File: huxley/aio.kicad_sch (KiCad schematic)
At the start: 61 parts, among them J11 SMA_RF2-04A-T-00-50-G, J13 SMA_RF2-04A-T-00-50-G, J15 SMA_RF2-04A-T-00-50-G, J17 SMA_RF2-04A-T-00-50-G, J18 SMA_RF2-04A-T-00-50-G, J19 SMA_RF2-04A-T-00-50-G, J20 SMA_RF2-04A-T-00-50-G, J22 SMA_RF2-04A-T-00-50-G, J24 CT3151V1-2, J39 CT3151V1-2, J4 SMA_RF2-04A-T-00-50-G, J7 SMA_RF2-04A-T-00-50-G, J9 SMA_RF2-04A-T-00-50-G

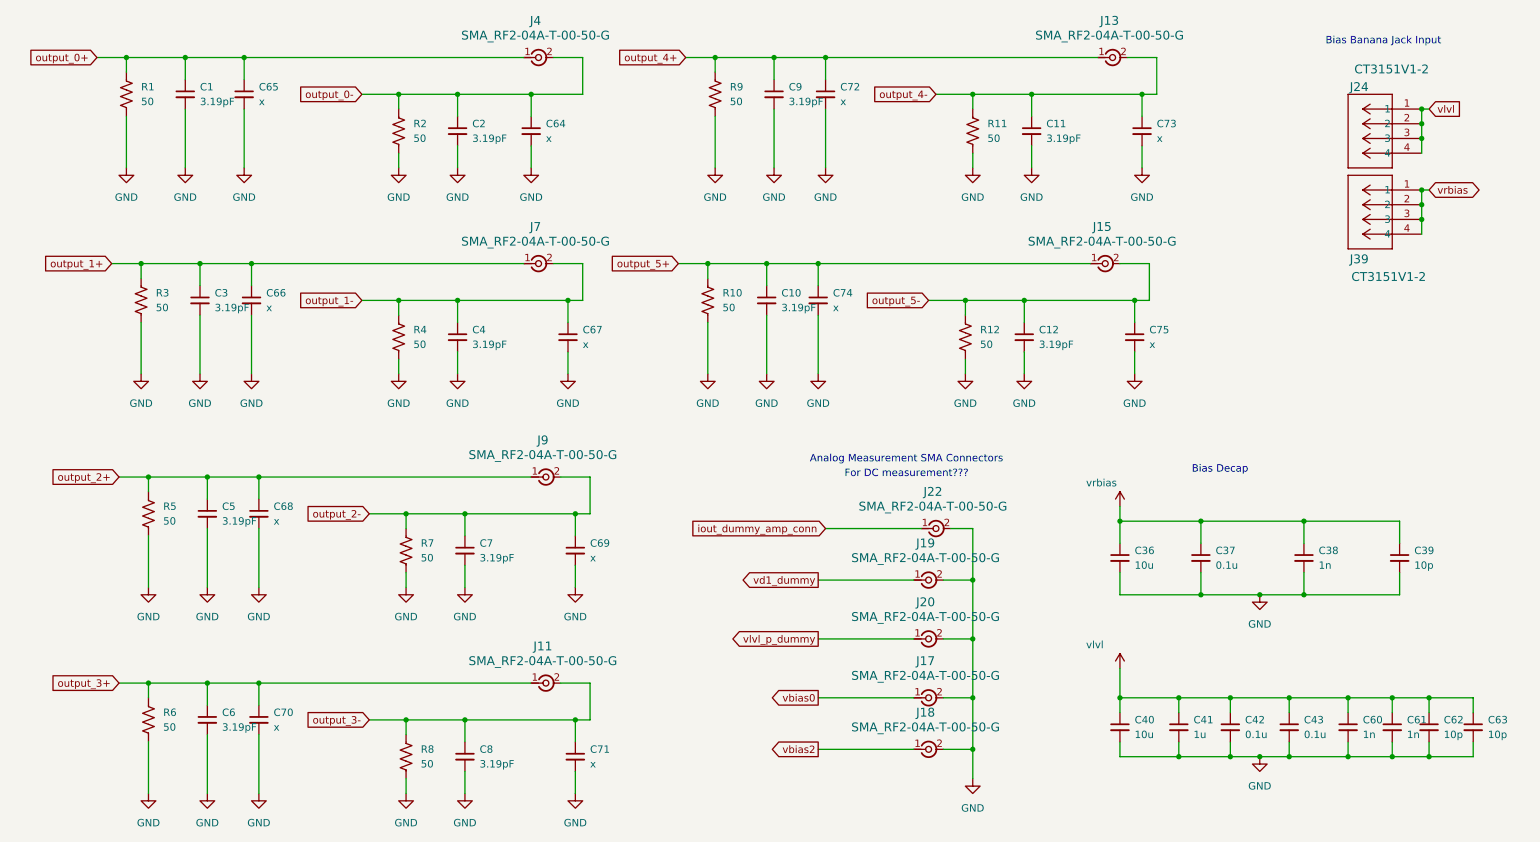
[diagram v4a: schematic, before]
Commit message: added DNP prop to some caps and updated bom; added regular and rounded board outputs
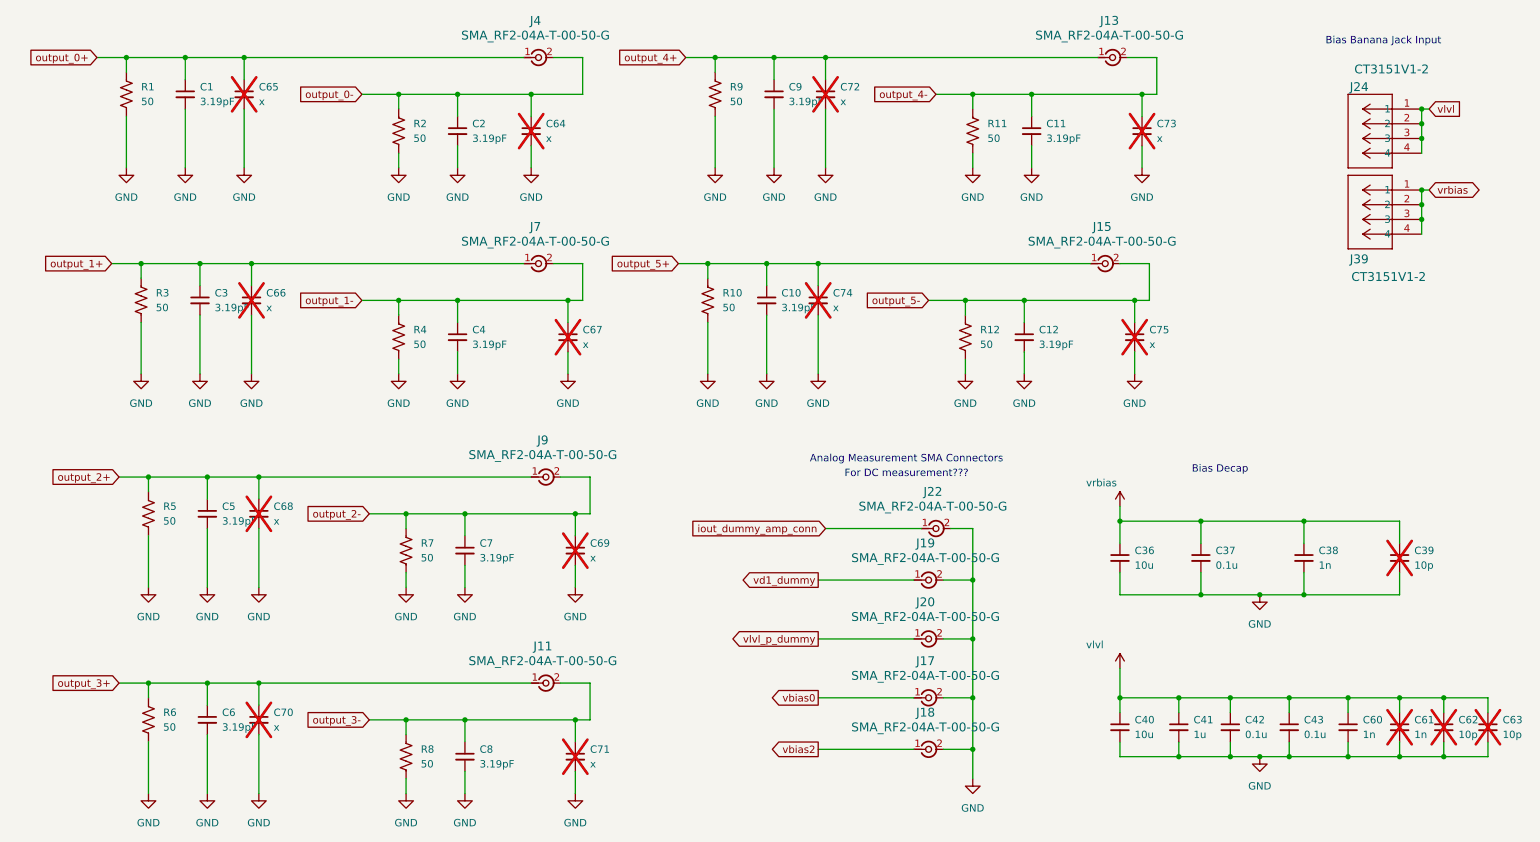
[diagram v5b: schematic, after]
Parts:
- C39, C61, C62, C63, C64, C65, C66, C67, C68, C69, C70, C71, C72, C73, C74, C75: now not fitted
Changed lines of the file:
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@@
 	)
 	(junction
-		(at 255.27 152.4)
+		(at 256.54 152.4)
 		(diameter 0)
 		(color 0 0 0 0)
@@
 	)
 	(junction
-		(at 255.27 142.24)
+		(at 256.54 142.24)
 		(diameter 0)
 		(color 0 0 0 0)
@@
 	)
 	(junction
+		(at 264.16 152.4)
+		(diameter 0)
+		(color 0 0 0 0)
+	)
+	(junction
 		(at 85.09 146.05)
 		(diameter 0)
@@
 	)
 	(junction
+		(at 264.16 142.24)
+		(diameter 0)
+		(color 0 0 0 0)
+	)
+	(junction
 		(at 83.82 38.1)
 		(diameter 0)
@@
 	)
 	(junction
-		(at 261.62 152.4)
-		(diameter 0)
-		(color 0 0 0 0)
-	)
-	(junction
 		(at 260.35 54.61)
 		(diameter 0)
@@
 		(color 0 0 0 0)
 	)
-	(junction
-		(at 261.62 142.24)
-		(diameter 0)
-		(color 0 0 0 0)
-	)
 	(wire
 		(pts
@@
 	(wire
 		(pts
-			(xy 269.24 152.4) (xy 261.62 152.4)
+			(xy 271.78 152.4) (xy 264.16 152.4)
 		)
 		(stroke
@@
 	(wire
 		(pts
-			(xy 247.65 142.24) (xy 255.27 142.24)
+			(xy 247.65 142.24) (xy 256.54 142.24)
 		)
 		(stroke
@@
 	(wire
 		(pts
-			(xy 269.24 142.24) (xy 261.62 142.24)
+			(xy 271.78 142.24) (xy 264.16 142.24)
 		)
 		(stroke
@@
 	(wire
 		(pts
-			(xy 255.27 149.86) (xy 255.27 152.4)
+			(xy 256.54 149.86) (xy 256.54 152.4)
 		)
 		(stroke
@@
 	(wire
 		(pts
-			(xy 269.24 149.86) (xy 269.24 152.4)
+			(xy 271.78 149.86) (xy 271.78 152.4)
 		)
 		(stroke
@@
 	(wire
 		(pts
-			(xy 261.62 149.86) (xy 261.62 152.4)
+			(xy 264.16 149.86) (xy 264.16 152.4)
 		)
 		(stroke
@@
 	(wire
 		(pts
-			(xy 247.65 152.4) (xy 255.27 152.4)
+			(xy 247.65 152.4) (xy 256.54 152.4)
 		)
 		(stroke
@@
 	(wire
 		(pts
-			(xy 255.27 142.24) (xy 261.62 142.24)
+			(xy 256.54 142.24) (xy 264.16 142.24)
 		)
 		(stroke
@@
 	(wire
 		(pts
-			(xy 255.27 144.78) (xy 255.27 142.24)
+			(xy 256.54 144.78) (xy 256.54 142.24)
 		)
 		(stroke
@@
 	(wire
 		(pts
-			(xy 255.27 152.4) (xy 261.62 152.4)
+			(xy 256.54 152.4) (xy 264.16 152.4)
 		)
 		(stroke
@@
 	(wire
 		(pts
-			(xy 269.24 144.78) (xy 269.24 142.24)
+			(xy 271.78 144.78) (xy 271.78 142.24)
 		)
 		(stroke
@@
 	(wire
 		(pts
-			(xy 261.62 144.78) (xy 261.62 142.24)
+			(xy 264.16 144.78) (xy 264.16 142.24)
 		)
 		(stroke
@@
 		(in_bom yes)
 		(on_board yes)
-		(dnp no)
+		(dnp yes)
 		(fields_autoplaced yes)
 		(property "Reference" "C75"
@@
 	(symbol
 		(lib_id "Device:C_Small")
-		(at 261.62 147.32 0)
+		(at 264.16 147.32 0)
 		(unit 1)
 		(exclude_from_sim no)
 		(in_bom yes)
 		(on_board yes)
-		(dnp no)
+		(dnp yes)
 		(fields_autoplaced yes)
 		(property "Reference" "C62"
-			(at 264.16 146.0562 0)
+			(at 266.7 146.0562 0)
 			(effects
 				(font
@@
 		)
 		(property "Value" "10p"
-			(at 264.16 148.5962 0)
+			(at 266.7 148.5962 0)
 			(effects
 				(font
@@
 		)
 		(property "Footprint" "Capacitor_SMD:C_0603_1608Metric"
-			(at 261.62 147.32 0)
+			(at 264.16 147.32 0)
 			(effects
 				(font
@@
 		)
 		(property "Datasheet" "~"
-			(at 261.62 147.32 0)
+			(at 264.16 147.32 0)
 			(effects
 				(font
@@
 		)
 		(property "Description" "Unpolarized capacitor, small symbol"
-			(at 261.62 147.32 0)
+			(at 264.16 147.32 0)
 			(effects
 				(font
@@
 	(symbol
 		(lib_id "Device:C_Small")
-		(at 255.27 147.32 0)
+		(at 256.54 147.32 0)
 		(unit 1)
 		(exclude_from_sim no)
 		(in_bom yes)
 		(on_board yes)
-		(dnp no)
+		(dnp yes)
 		(property "Reference" "C61"
-			(at 257.81 146.0562 0)
+			(at 259.08 146.0562 0)
 			(effects
 				(font
@@
 		)
 		(property "Value" "1n"
-			(at 257.81 148.5962 0)
+			(at 259.08 148.5962 0)
 			(effects
 				(font
@@
 		)
 		(property "Footprint" "Capacitor_SMD:C_0603_1608Metric"
-			(at 255.27 147.32 0)
+			(at 256.54 147.32 0)
 			(effects
 				(font
@@
 		)
 		(property "Datasheet" "~"
-			(at 255.27 147.32 0)
+			(at 256.54 147.32 0)
 			(effects
 				(font
@@
 		)
 		(property "Description" "Unpolarized capacitor, small symbol"
-			(at 255.27 147.32 0)
+			(at 256.54 147.32 0)
 			(effects
 				(font
@@
 	(symbol
 		(lib_id "Device:C_Small")
-		(at 269.24 147.32 0)
+		(at 271.78 147.32 0)
 		(unit 1)
 		(exclude_from_sim no)
 		(in_bom yes)
 		(on_board yes)
-		(dnp no)
+		(dnp yes)
 		(fields_autoplaced yes)
 		(property "Reference" "C63"
-			(at 271.78 146.0562 0)
+			(at 274.32 146.0562 0)
 			(effects
 				(font
@@
 		)
 		(property "Value" "10p"
-			(at 271.78 148.5962 0)
+			(at 274.32 148.5962 0)
 			(effects
 				(font
@@
 		)
 		(property "Footprint" "Capacitor_SMD:C_0603_1608Metric"
-			(at 269.24 147.32 0)
+			(at 271.78 147.32 0)
 			(effects
 				(font
@@
 		)
 		(property "Datasheet" "~"
-			(at 269.24 147.32 0)
+			(at 271.78 147.32 0)
 			(effects
 				(font
@@
 		)
 		(property "Description" "Unpolarized capacitor, small symbol"
-			(at 269.24 147.32 0)
+			(at 271.78 147.32 0)
 			(effects
 				(font
@@
 		(in_bom yes)
 		(on_board yes)
-		(dnp no)
+		(dnp yes)
 		(fields_autoplaced yes)
 		(property "Reference" "C72"
@@
 		(in_bom yes)
 		(on_board yes)
-		(dnp no)
+		(dnp yes)
 		(fields_autoplaced yes)
 		(property "Reference" "C68"
@@
 		(in_bom yes)
 		(on_board yes)
-		(dnp no)
+		(dnp yes)
 		(fields_autoplaced yes)
 		(property "Reference" "C64"
@@
 		(in_bom yes)
 		(on_board yes)
-		(dnp no)
+		(dnp yes)
 		(fields_autoplaced yes)
 		(property "Reference" "C66"
@@
 		(in_bom yes)
 		(on_board yes)
-		(dnp no)
+		(dnp yes)
 		(fields_autoplaced yes)
 		(property "Reference" "C67"
@@
 		(in_bom yes)
 		(on_board yes)
-		(dnp no)
+		(dnp yes)
 		(fields_autoplaced yes)
 		(property "Reference" "C71"
@@
 		(in_bom yes)
 		(on_board yes)
-		(dnp no)
+		(dnp yes)
 		(fields_autoplaced yes)
 		(property "Reference" "C39"
@@
 		(in_bom yes)
 		(on_board yes)
-		(dnp no)
+		(dnp yes)
 		(fields_autoplaced yes)
 		(property "Reference" "C73"
@@
 		(in_bom yes)
 		(on_board yes)
-		(dnp no)
+		(dnp yes)
 		(fields_autoplaced yes)
 		(property "Reference" "C69"
@@
 		(in_bom yes)
 		(on_board yes)
-		(dnp no)
+		(dnp yes)
 		(fields_autoplaced yes)
 		(property "Reference" "C65"
@@
 		(in_bom yes)
 		(on_board yes)
-		(dnp no)
+		(dnp yes)
 		(fields_autoplaced yes)
 		(property "Reference" "C70"
@@
 		(in_bom yes)
 		(on_board yes)
-		(dnp no)
+		(dnp yes)
 		(fields_autoplaced yes)
 		(property "Reference" "C74"

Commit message: DFA fixes; bump huxley version number to v1.1.1; added updated BOM v1.1.1
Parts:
- R1, R10, R11, R12, R2, R3, R4, R5, R6, R7, R8, R9: footprint Resistor_SMD:R_0603_1608Metric -> 0_726_footprints:R_0603_1608Metric_Vishay_WBT
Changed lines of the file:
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@@
 			)
 		)
-		(property "Footprint" "Resistor_SMD:R_0603_1608Metric"
+		(property "Footprint" "0_726_footprints:R_0603_1608Metric_Vishay_WBT"
 			(at 84.836 44.704 90)
 			(effects
@@
 			)
 		)
-		(property "Footprint" "Resistor_SMD:R_0603_1608Metric"
+		(property "Footprint" "0_726_footprints:R_0603_1608Metric_Vishay_WBT"
 			(at 40.386 73.914 90)
 			(effects
@@
 			)
 		)
-		(property "Footprint" "Resistor_SMD:R_0603_1608Metric"
+		(property "Footprint" "0_726_footprints:R_0603_1608Metric_Vishay_WBT"
 			(at 86.106 152.654 90)
 			(effects
@@
 			)
 		)
-		(property "Footprint" "Resistor_SMD:R_0603_1608Metric"
+		(property "Footprint" "0_726_footprints:R_0603_1608Metric_Vishay_WBT"
 			(at 41.656 110.744 90)
 			(effects
@@
 			)
 		)
-		(property "Footprint" "Resistor_SMD:R_0603_1608Metric"
+		(property "Footprint" "0_726_footprints:R_0603_1608Metric_Vishay_WBT"
 			(at 183.896 44.704 90)
 			(effects
@@
 			)
 		)
-		(property "Footprint" "Resistor_SMD:R_0603_1608Metric"
+		(property "Footprint" "0_726_footprints:R_0603_1608Metric_Vishay_WBT"
 			(at 138.176 73.914 90)
 			(effects
@@
 			)
 		)
-		(property "Footprint" "Resistor_SMD:R_0603_1608Metric"
+		(property "Footprint" "0_726_footprints:R_0603_1608Metric_Vishay_WBT"
 			(at 41.656 146.304 90)
 			(effects
@@
 			)
 		)
-		(property "Footprint" "Resistor_SMD:R_0603_1608Metric"
+		(property "Footprint" "0_726_footprints:R_0603_1608Metric_Vishay_WBT"
 			(at 86.106 117.094 90)
 			(effects
@@
 			)
 		)
-		(property "Footprint" "Resistor_SMD:R_0603_1608Metric"
+		(property "Footprint" "0_726_footprints:R_0603_1608Metric_Vishay_WBT"
 			(at 37.846 38.354 90)
 			(effects
@@
 			)
 		)
-		(property "Footprint" "Resistor_SMD:R_0603_1608Metric"
+		(property "Footprint" "0_726_footprints:R_0603_1608Metric_Vishay_WBT"
 			(at 139.446 38.354 90)
 			(effects
@@
 			)
 		)
-		(property "Footprint" "Resistor_SMD:R_0603_1608Metric"
+		(property "Footprint" "0_726_footprints:R_0603_1608Metric_Vishay_WBT"
 			(at 182.626 80.264 90)
 			(effects
@@
 			)
 		)
-		(property "Footprint" "Resistor_SMD:R_0603_1608Metric"
+		(property "Footprint" "0_726_footprints:R_0603_1608Metric_Vishay_WBT"
 			(at 84.836 80.264 90)
 			(effects
